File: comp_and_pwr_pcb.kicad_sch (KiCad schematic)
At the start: 143 parts, among them IC1 TPS5430MDDAREP, IC2 ICM-42688-P, IC3 LTC4415EDHC#TRPBF, IC4 TPS259531DSGR, IC5 BMP388, IC6 W25Q32JVSSIQ, J1 USB4216-03-A, J10 Conn_01x02, J11 Conn_Coaxial, J12 Conn_Coaxial, J2 BATTERY_CONN, J3 SWD_CONN, J4 SERVO_CONN_01, J5 SERVO_CONN_02, J6 DM3AT-SF-PEJM5, J7 CAMERA_CONN_01, J8 CAMERA_CONN_02, J9 Conn_01x02, Q1 2N3904, Q2 BSS138, Q3 BSS138, Q4 BC847B, Q5 BC847B, Q6 MMBT3904, Q7 MMBT3904, SW1 SW_Push, SW2 SW_Push, U1 RP2040, U2 MAX-M10S, U3 MP2307DN-LF-Z, Y1 ABMM2-12.000MHZ-D1-T

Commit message: Changes
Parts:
- removed C14, C22: 10uF, Capacitor_SMD:C_0402_1005Metric, symbol Device:C_Small
- removed C21, C25: 100nF, Capacitor_SMD:C_0402_1005Metric, symbol Device:C_Small
- removed IC2: ICM-42688-P, ICM-42688-P:IIM42352, symbol ICM-42688-P:ICM-42688-P
- removed JP4: SolderJumper_3_Open, Jumper:SolderJumper-3_P1.3mm_Open_Pad1.0x1.5mm, symbol Jumper:SolderJumper_3_Open
- removed Q6, Q7: MMBT3904, Package_TO_SOT_SMD:SOT-23, symbol Transistor_BJT:MMBT3904
- added C26, C32: 100nF, Capacitor_SMD:C_0402_1005Metric, symbol Device:C_Small
- added C27, C31: 10uF, Capacitor_SMD:C_0402_1005Metric, symbol Device:C_Small
- added JP2: SolderJumper_3_Open, Jumper:SolderJumper-3_P1.3mm_Open_Pad1.0x1.5mm, symbol Jumper:SolderJumper_3_Open
- added Q6, Q8: DMP3013SFV, Package_SON:Diodes_PowerDI3333-8, symbol Transistor_FET:DMP3013SFV
- added U4: LSM6DSO, LSM6DSO:LGA14L, symbol LSM6DSO:LSM6DSO
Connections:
- net +3.3V: now also C26.2, C27.2, C31.2, C32.1, JP2.1 (A), U4.12 (~{CS}), U4.5 (VDDIO), U4.8 (VDD)
- net +BATT: now also Q6.1 (S), Q6.2 (S), Q6.3 (S), Q8.1 (S), Q8.2 (S), Q8.3 (S)
- net GND: now also C26.1, C27.1, C31.1, C32.2, JP2.3 (B), U4.6 (GND@6), U4.7 (GND@7)
- net I2C_SCL: now also U4.13 (SCL)
- net I2C_SDA: now also U4.14 (SDA)
- net at J9.1 (Pin_1), R64.1: now also Q6.5 (D)
- net at R58.1: now also Q8.4 (G)
- net at J10.1 (Pin_1), R60.1: now also Q8.5 (D)
- net at R62.1: now also Q6.4 (G)
- new net: JP2.2 (C), U4.1 (SDO/SA0)
- no-connect marks 41 -> 40

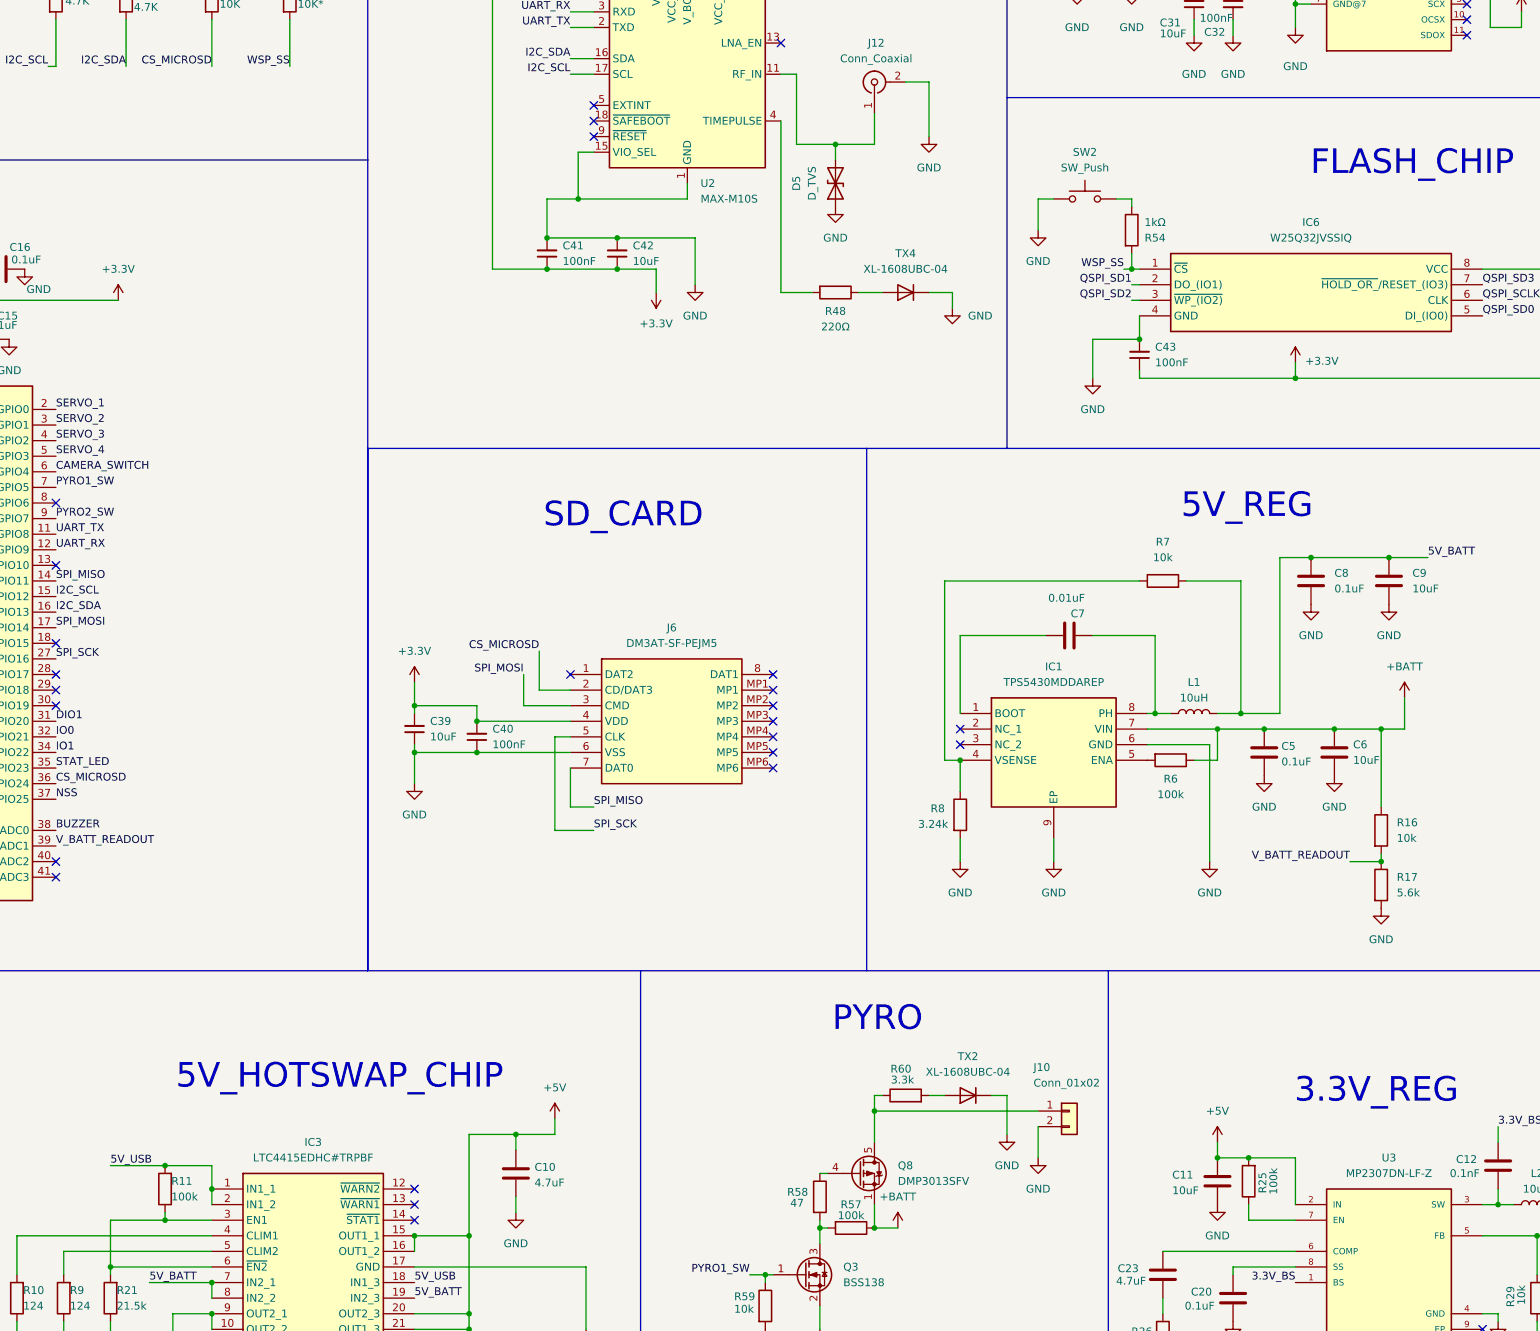
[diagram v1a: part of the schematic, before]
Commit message: added MPN and manufacturer
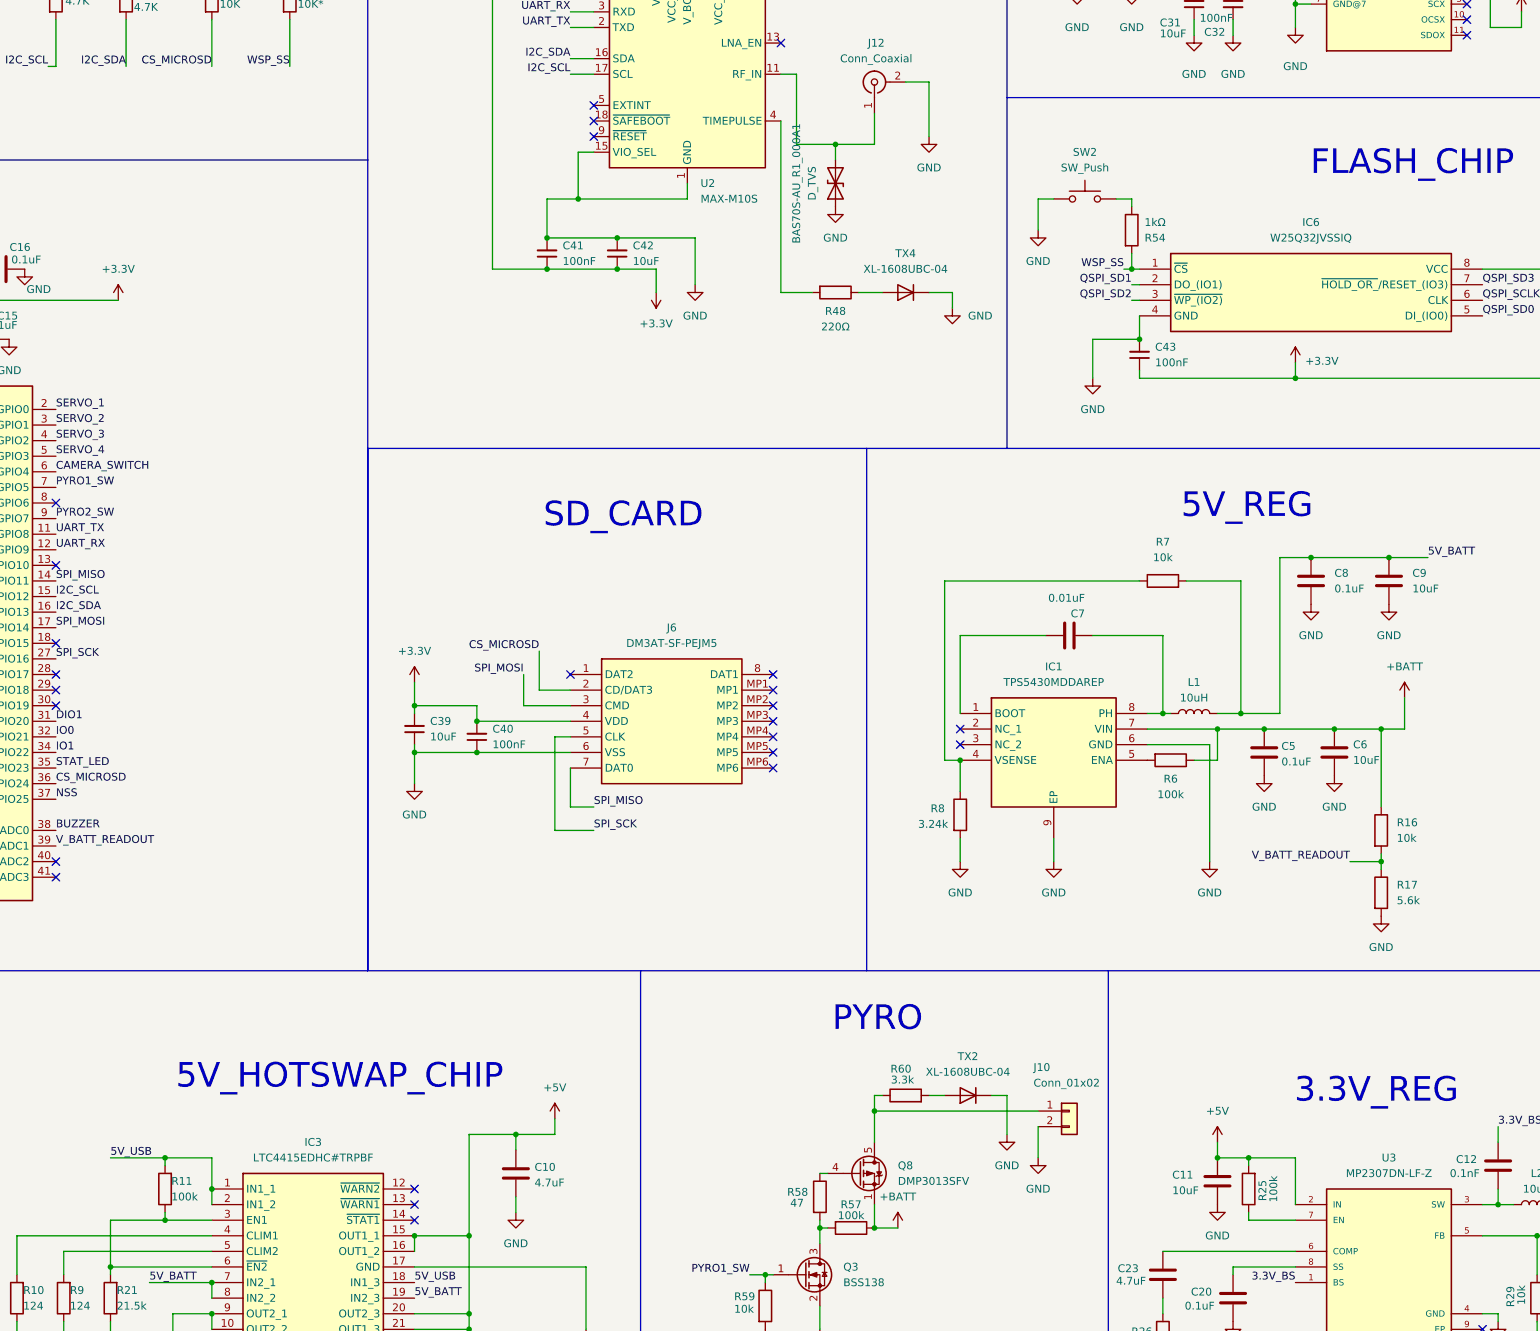
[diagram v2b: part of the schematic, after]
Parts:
- BAS70S-AU_R1_000A1: renamed from D5; MPN (none) -> BAS70S-AU_R1_000A1; Manufacturer (none) -> Panjit
- BZ1: MPN (none) -> CPT-9019S-SMT-TR; Manufacturer (none) -> Same Sky
- C1, C3: MPN (none) -> C0402C300F5GAC; Manufacturer (none) -> KEMET
- C10, C23: MPN (none) -> C0805C475K8PACTU; Manufacturer (none) -> KEMET
- C11, C13, C2, C24, C27, C31, C35, C39, C42, C6, C9: MPN (none) -> C0402C106M9PACTU; Manufacturer (none) -> KEMET
- C12, C16, C17, C18, C4: MPN (none) -> C0402C104K4RAC7411; Manufacturer (none) -> Yageo
- C15, C19: MPN (none) -> C0402C105K8PACTU; Manufacturer (none) -> KEMET
- C20, C26, C28, C29, C32, C34, C38, C40, C41, C43, C5, C52, C8: MPN (none) -> C0402C104K4RAC7411; Manufacturer (none) -> KEMET
- C30: MPN (none) -> 6TPF470MFH; Manufacturer (none) -> Panasonic
- C36: MPN (none) -> T495X476K020AHE150; Manufacturer (none) -> KEMET
- C51: MPN (none) -> KEMET; Manufacturer (none) -> C0402C104K4RAC7411
- C7: MPN (none) -> GRM1555C1H101FA01D; Manufacturer (none) -> Murata Electronics
- D1, D2: MPN (none) -> ESD5Z5.0T1G; Manufacturer (none) -> onsemi
- D3: MPN (none) -> BAS70S-AU_R1_000A1; Manufacturer (none) -> Panjit
- D4: MPN (none) -> SZSMF6L5.0AT3G; Manufacturer (none) -> Littelfuse
- F1: MPN (none) -> 0ABA-1000-TN; Manufacturer (none) -> Bel Fuse
- F2: MPN (none) -> 2016L200PR; Manufacturer (none) -> Littelfuse
- IC1: MPN (none) -> TPS5430MDDAREP; Manufacturer (none) -> Texas Instruments
- IC3: MPN (none) -> LTC4415EDHC#TRPBF; Manufacturer (none) -> Analog Devices
- IC4: MPN (none) -> TPS259531DSGR; Manufacturer (none) -> Texas Instruments
- IC5: MPN (none) -> BMP388; Manufacturer (none) -> Bosch
- IC6: MPN (none) -> W25Q32JVSSIQ; Manufacturer (none) -> Winbond
- J1: MPN (none) -> USB4216-03-A; Manufacturer (none) -> GCT
- J10, J2, J7, J8, J9: MPN (none) -> 284514-2; Manufacturer (none) -> TE Connectivity
- J11, J12: MPN (none) -> 73251-2200; Manufacturer (none) -> Molex
- J3: MPN (none) -> M20-9990546; Manufacturer (none) -> Harwin
- J4, J5: MPN (none) -> 90131-0763; Manufacturer (none) -> Molex
- J6: MPN (none) -> DM3AT-SF-PEJM5; Manufacturer (none) -> Hirose Connector
- L1, L2: MPN (none) -> 74437349033; Manufacturer (none) -> Wurth Elektronik
- Q1: MPN (none) -> MMBT3904; Manufacturer (none) -> Diotec Semiconductor
- Q2, Q3: MPN (none) -> BSS138; Manufacturer (none) -> onsemi / Fairchild
- Q4, Q5: MPN (none) -> BC847B; Manufacturer (none) -> Diotec Semiconductor
- Q6, Q8: MPN (none) -> DMP3013SFV-7; Manufacturer (none) -> Diodes Incorporated
- R1, R14, R20: MPN (none) -> RC0402FR‑071KL; Manufacturer (none) -> Yageo
- R10, R9: MPN (none) -> RC0402FR-07124RL; Manufacturer (none) -> Yageo
- R11, R25, R57, R6, R63: MPN (none) -> RC0402FR-07100KL; Manufacturer (none) -> Yageo
- R12, R13: MPN (none) -> RC0402JR-7D33RL; Manufacturer (none) -> Yageo
- R15, R16, R29, R30, R39, R40, R45, R59, R61, R7: MPN (none) -> RC0402FR-0710KL; Manufacturer (none) -> Yageo
- R17: MPN (none) -> RC0402FR-075K6L; Manufacturer (none) -> Yageo
- R19, R22, R23: MPN (none) -> RC1206FR-07100RL; Manufacturer (none) -> Yageo
- R2, R3: MPN (none) -> RC0402FR-075K1L; Manufacturer (none) -> Yageo
- R21: MPN (none) -> RC0402FR-0721K5L; Manufacturer (none) -> Yageo
- R24: MPN (none) -> RC0402FR-075K76L; Manufacturer (none) -> Yageo
- R26: MPN (none) -> RC0402FR-076K8L; Manufacturer (none) -> Yageo
- R27: MPN (none) -> RC0402FR-0726K1L; Manufacturer (none) -> Yageo
- R32: MPN (none) -> RC0603FR-0715K8L; Manufacturer (none) -> Yageo
- R35, R36, R37, R38: MPN (none) -> RC0402FR-07100RL; Manufacturer (none) -> Yageo
- R4, R5: MPN (none) -> RC0402FR-0722RL; Manufacturer (none) -> Yageo
- R41, R42: MPN (none) -> RC0402FR-07220R; Manufacturer (none) -> Yageo
- R43, R44: MPN (none) -> RC0402FR-074K7L; Manufacturer (none) -> Yageo
- R48: MPN (none) -> RC0402FR-07220RL; Manufacturer (none) -> Yageo
- R54: MPN (none) -> RC0402FR-071KL; Manufacturer (none) -> Yageo
- R58, R62: MPN (none) -> RC0402FR-0747RL; Manufacturer (none) -> Yageo
- R60, R64: MPN (none) -> RC0402FR-073K3L; Manufacturer (none) -> Yageo
- R8: MPN (none) -> RC0402FR-073R24L; Manufacturer (none) -> Yageo
- STATUS1: MPN (none) -> COM-24837; Manufacturer (none) -> SparkFun
- SW1, SW2: MPN (none) -> PTS645SM43SMTR92; Manufacturer (none) -> C&K
- TX1, TX2, TX3, TX4: MPN (none) -> XL-1608UBC-04; Manufacturer (none) -> XINGLIGHT
- U1: MPN (none) -> RP2040; Manufacturer (none) -> Raspberry Pi
- U2: MPN (none) -> MAX-M10S-00B; Manufacturer (none) -> u-blox
- U3: MPN (none) -> MP2307DN-LF-Z; Manufacturer (none) -> Monolithic Power Systems (MPS)
- U4: MPN (none) -> LSM6DSOTR; Manufacturer (none) -> STMicroelectronics
- Y1: MPN (none) -> ABMM2-12.000MHZ-D1-T; Manufacturer (none) -> ABRACON
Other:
- moved on the sheet: R17, R25
